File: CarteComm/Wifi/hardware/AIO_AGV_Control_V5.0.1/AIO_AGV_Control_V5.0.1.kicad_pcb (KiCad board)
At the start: 2 copper layers, 57 parts, among them J1 DB25_Pins, J2 DB25_Socket, T1 IRF520, T10 IRF520, T11 IRF520, T12 IRF520, T14 IRF520, T15 IRF520, T16 IRF520, T17 IRF520, T18 IRF520, T19 IRF520, T2 IRF520, T20 IRF520, T21 IRF520, T22 IRF520, T23 IRF520, T24 IRF520, T3 IRF520, T4 IRF520, T5 IRF520, T6 IRF520, T7 IRF520, T8 IRF520, T9 IRF520, U1 ESP32-DEVKITC

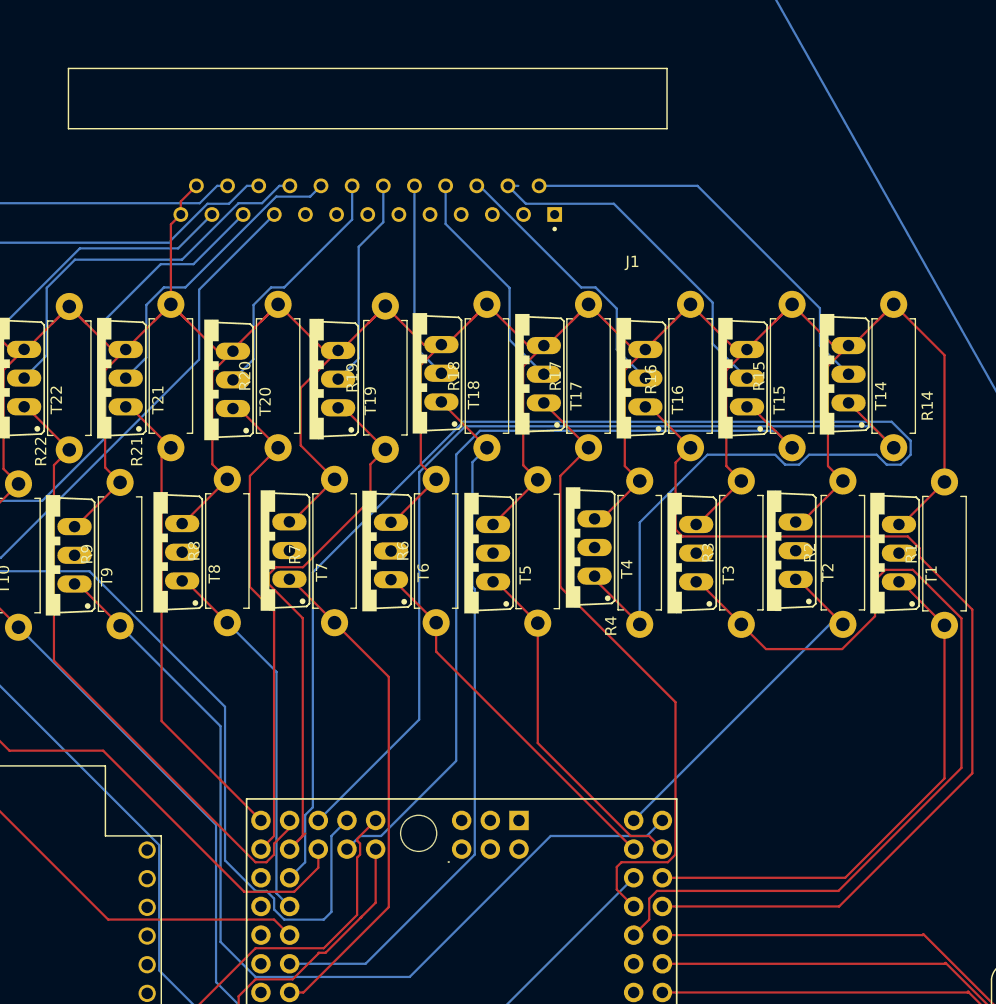
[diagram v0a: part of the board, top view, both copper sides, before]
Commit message: test(lora): essais radio d'émission et de réception, côté ESP32 et côté Linux
Deux sous-dossiers dans LoRa/test/, chacun avec un essai d'émission et un de
réception, donc quatre combinaisons possibles. Les deux croisées - ESP32 vers
Linux et Linux vers ESP32 - sont les seules qui prouvent quelque chose : une
implémentation confrontée à elle-même ne démontre que sa propre cohérence.

Le point de conception est là. Une radio qui porte et des trames qui divergent
d'un bit donnent un banc parfait et une panne en atelier, alors les deux côtés
parlent la trame applicative du projet, pas un message d'essai. Côté ESP32 les
sketches compilent le pilote Sx1276Radio et le DutyCycleBudget du dépôt ; côté
Linux, agv_frame.py est un portage fidèle de frame.cpp.

Ce portage n'est pas pris sur parole : test_interop_trame.py compile le codec
C++ du coeur, lui fait produire des vecteurs et compare octet à octet. Six
vecteurs, extension d'horodatage comprise, zéro écart. C'est le seul essai du
dossier qui tourne sans matériel.

Le budget de rapport cyclique est appliqué des deux côtés, accusés compris - un
récepteur qui acquitte est un émetteur. Les deux essais de réception alertent
sous -115 dBm de RSSI : un lien qui passe tout juste ne passe pas une fois un
chariot chargé entre les antennes.

Le brochage ESP32 par défaut reprend les broches relevées libres au KiCad, avec
un static_assert contre IO16 et IO17 qui portent la liaison vers le MEGA.

Le README rappelle qu'un Gate G100 ne peut pas faire tourner les scripts unipi :
boîtier fermé, ni SPI ni GPIO.

Co-Authored-By: Claude Opus 5 <noreply@anthropic.com>
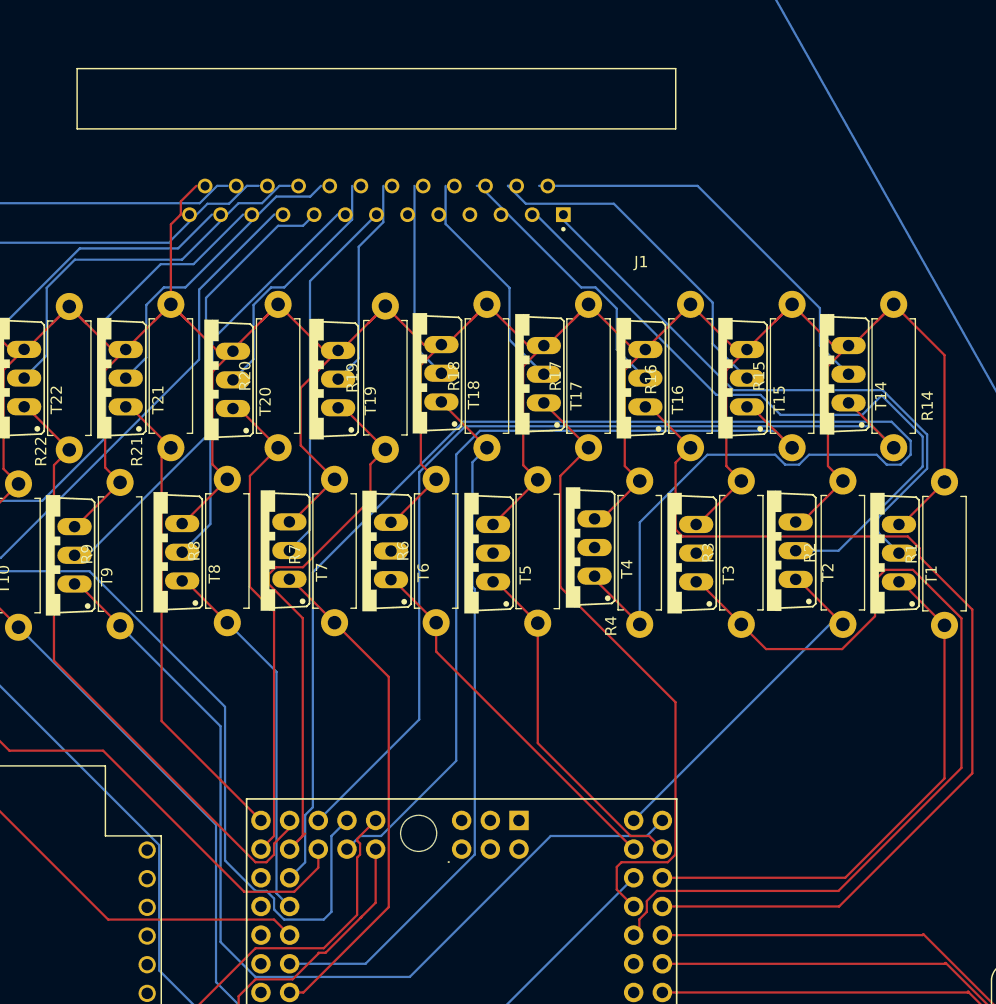
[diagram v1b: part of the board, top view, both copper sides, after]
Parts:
- moved J1 0.77 mm to (99.7, 31.7)
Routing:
- net Net-(J1-Pad2): track 0.00 -> 61.2 mm
- net Net-(J1-Pad1): track 0.00 -> 53.6 mm
- net Net-(J1-Pad9): track 0.00 -> 40.9 mm
- net Net-(J1-Pad8): track 0.00 -> 36.3 mm
- net Net-(J1-Pad7): track 0.00 -> 32.9 mm
